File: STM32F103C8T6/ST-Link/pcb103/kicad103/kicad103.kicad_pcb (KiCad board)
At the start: 2 copper layers, 1 part, among them J1 0480372200

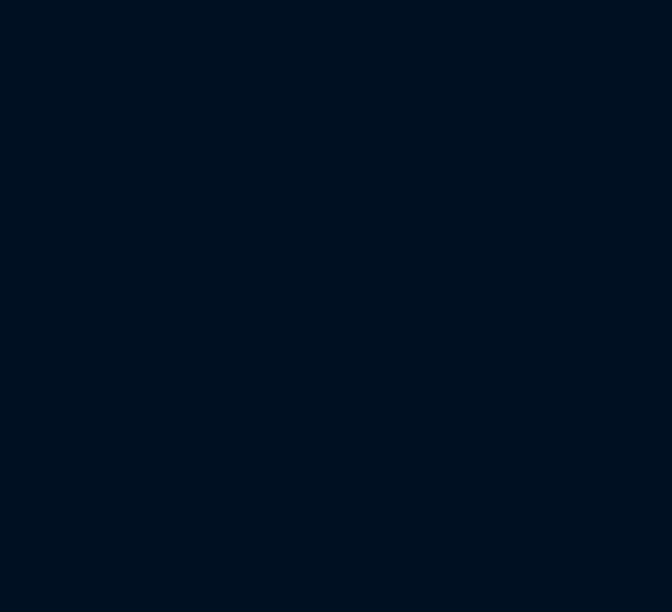
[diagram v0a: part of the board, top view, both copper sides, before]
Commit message: Add 3.3V LDO
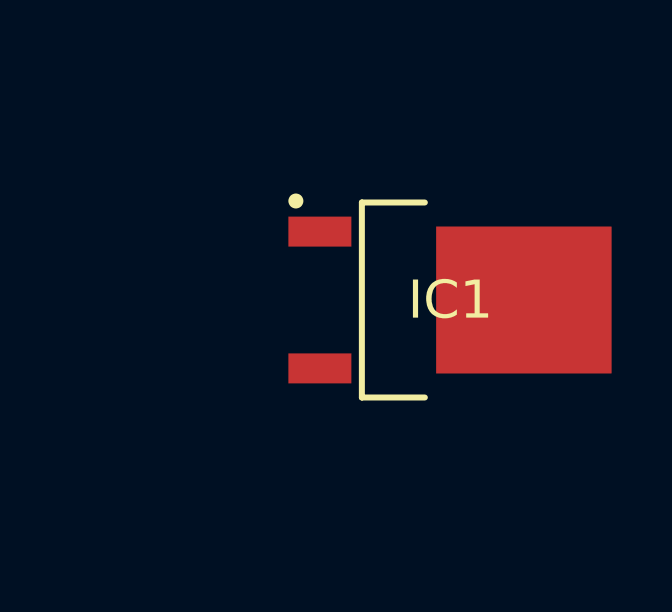
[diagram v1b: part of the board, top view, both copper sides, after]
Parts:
- added IC1: LD1117DT33TR, Library:TO228P972X240-3N, F.Cu at (236.3, 74.2)
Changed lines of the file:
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@@
   (net 7 "unconnected-(J1-Pad7)")
   (net 8 "unconnected-(J1-Pad8)")
+  (net 9 "unconnected-(IC1-GND-Pad1)")
+  (net 10 "unconnected-(IC1-VIN-Pad3)")
+  (net 11 "unconnected-(IC1-(THERMALPAD)-Pad4)")
+  (footprint "Library:TO228P972X240-3N" (layer "F.Cu")
+    (at 236.35 74.2)
+    (descr "DPAK (TO-252)")
+    (tags "Integrated Circuit")
+    (property "Arrow Part Number" "LD1117DT33TR")
+    (property "Arrow Price/Stock" "https://www.arrow.com/en/products/ld1117dt33tr/stmicroelectronics?region=nac")
+    (property "Height" "2.4")
+    (property "Manufacturer_Name" "STMicroelectronics")
+    (property "Manufacturer_Part_Number" "LD1117DT33TR")
+    (property "Mouser Part Number" "511-LD1117DT33-TR")
+    (property "Mouser Price/Stock" "https://www.mouser.co.uk/ProductDetail/STMicroelectronics/LD1117DT33TR?qs=4JhUBQGAOSd4P5jVYGxp2g%3D%3D")
+    (property "Sheetfile" "kicad103.kicad_sch")
+    (property "Sheetname" "")
+    (property "ki_description" "LDO Regulator 3.3V 1.3A DPAK STMicroelectronics LD1117DT33TR, LDO Voltage Regulator, 1.3A, 3.3 V +/-1%, 3-Pin DPAK")
+    (attr smd)
+    (fp_text reference "IC1" (at 0 0) (layer "F.SilkS")
+        (effects (font (size 1.27 1.27) (thickness 0.254)))
+    )
+    (fp_text value "LD1117DT33TR" (at 0 0) (layer "F.SilkS") hide
+        (effects (font (size 1.27 1.27) (thickness 0.254)))
+    )
+    (fp_text user "${REFERENCE}" (at 0 0) (layer "F.Fab")
+        (effects (font (size 1.27 1.27) (thickness 0.254)))
+    )
+    (fp_line (start -2.95 -3.25) (end -0.85 -3.25)
+      (stroke (width 0.2) (type solid)) (layer "F.SilkS"))
+    (fp_line (start -2.95 3.25) (end -2.95 -3.25)
+      (stroke (width 0.2) (type solid)) (layer "F.SilkS"))
+    (fp_line (start -0.85 3.25) (end -2.95 3.25)
+      (stroke (width 0.2) (type solid)) (layer "F.SilkS"))
+    (fp_circle (center -5.15 -3.3) (end -5.15 -3.175)
+      (stroke (width 0.25) (type solid)) (fill none) (layer "F.SilkS"))
+    (fp_line (start -5.65 -3.55) (end -5.65 3.55)
+      (stroke (width 0.05) (type solid)) (layer "F.CrtYd"))
+    (fp_line (start -5.65 3.55) (end 5.65 3.55)
+      (stroke (width 0.05) (type solid)) (layer "F.CrtYd"))
+    (fp_line (start -2.088 -3.3) (end -2.088 3.3)
+      (stroke (width 0.001) (type solid)) (layer "F.CrtYd"))
+    (fp_line (start -2.088 3.3) (end 4.112 3.3)
+      (stroke (width 0.001) (type solid)) (layer "F.CrtYd"))
+    (fp_line (start -0.5 0) (end 0.5 0)
+      (stroke (width 0.05) (type solid)) (layer "F.CrtYd"))
+    (fp_line (start 0 0.5) (end 0 -0.5)
+      (stroke (width 0.05) (type solid)) (layer "F.CrtYd"))
+    (fp_line (start 4.112 -3.3) (end -2.088 -3.3)
+      (stroke (width 0.001) (type solid)) (layer "F.CrtYd"))
+    (fp_line (start 4.112 3.3) (end 4.112 -3.3)
+      (stroke (width 0.001) (type solid)) (layer "F.CrtYd"))
+    (fp_line (start 5.65 -3.55) (end -5.65 -3.55)
+      (stroke (width 0.05) (type solid)) (layer "F.CrtYd"))
+    (fp_line (start 5.65 3.55) (end 5.65 -3.55)
+      (stroke (width 0.05) (type solid)) (layer "F.CrtYd"))
+    (fp_line (start -2.037 -3.25) (end -2.037 3.25)
+      (stroke (width 0.1) (type solid)) (layer "F.Fab"))
+    (fp_line (start -2.037 3.25) (end 4.062 3.25)
+      (stroke (width 0.1) (type solid)) (layer "F.Fab"))
+    (fp_line (start 4.062 -3.25) (end -2.037 -3.25)
+      (stroke (width 0.1) (type solid)) (layer "F.Fab"))
+    (fp_line (start 4.062 2.35) (end 4.326 2.35)
+      (stroke (width 0.1) (type solid)) (layer "F.Fab"))
+    (fp_line (start 4.062 3.25) (end 4.062 -3.25)
+      (stroke (width 0.1) (type solid)) (layer "F.Fab"))
+    (fp_line (start 4.326 2.35) (end 4.863 1.756)
+      (stroke (width 0.1) (type solid)) (layer "F.Fab"))
+    (fp_line (start 4.327 -2.35) (end 4.063 -2.35)
+      (stroke (width 0.1) (type solid)) (layer "F.Fab"))
+    (fp_line (start 4.863 -1.756) (end 4.327 -2.35)
+      (stroke (width 0.1) (type solid)) (layer "F.Fab"))
+    (fp_line (start 4.863 1.756) (end 4.863 -1.756)
+      (stroke (width 0.1) (type solid)) (layer "F.Fab"))
+    (pad "1" smd rect (at -4.35 -2.28 90) (size 1 2.1) (layers "F.Cu" "F.Paste" "F.Mask")
+      (net 9 "unconnected-(IC1-GND-Pad1)") (pinfunction "GND") (pintype "input"))
+    (pad "3" smd rect (at -4.35 2.28 90) (size 1 2.1) (layers "F.Cu" "F.Paste" "F.Mask")
+      (net 10 "unconnected-(IC1-VIN-Pad3)") (pinfunction "VIN") (pintype "output"))
+    (pad "4" smd rect (at 2.45 0 90) (size 4.9 5.85) (layers "F.Cu" "F.Paste" "F.Mask")
+      (net 11 "unconnected-(IC1-(THERMALPAD)-Pad4)") (pinfunction "(THERMALPAD)") (pintype "output"))
+    (model "/home/vovan/repos/bluepillfw/STM32F103C8T6/ST-Link/pcb103/mouser/lib/LD1117DT33TR.stp"
+      (offset (xyz 1.25 0 0))
+      (scale (xyz 1 1 1))
+      (rotate (xyz 0 0 90))
+    )
+  )
   (footprint "Library:0480372200" (layer "F.Cu")
     (at 211.95 77.375)

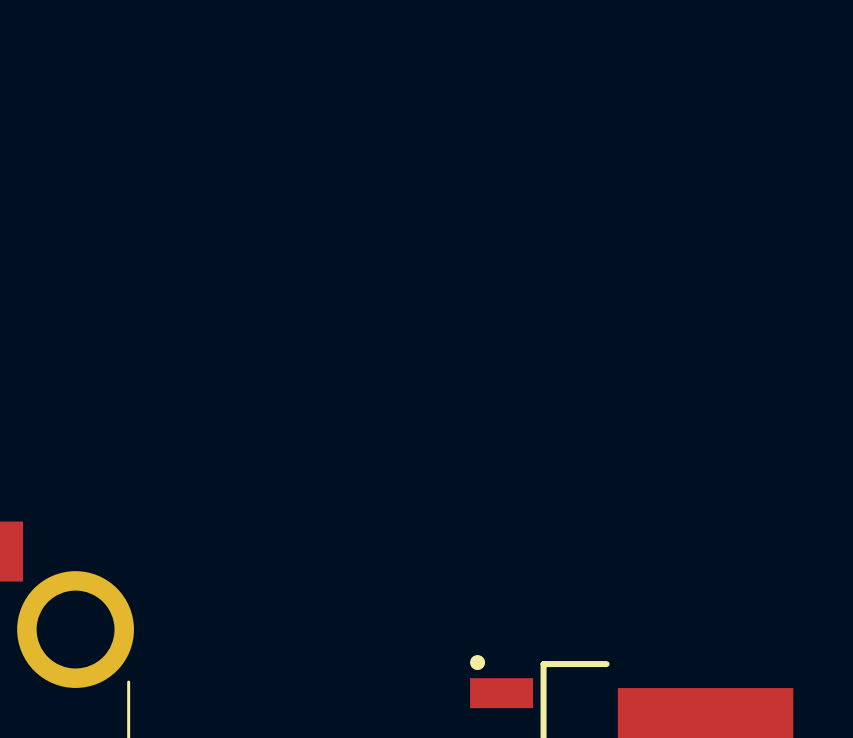
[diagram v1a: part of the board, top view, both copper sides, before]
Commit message: Add power LED
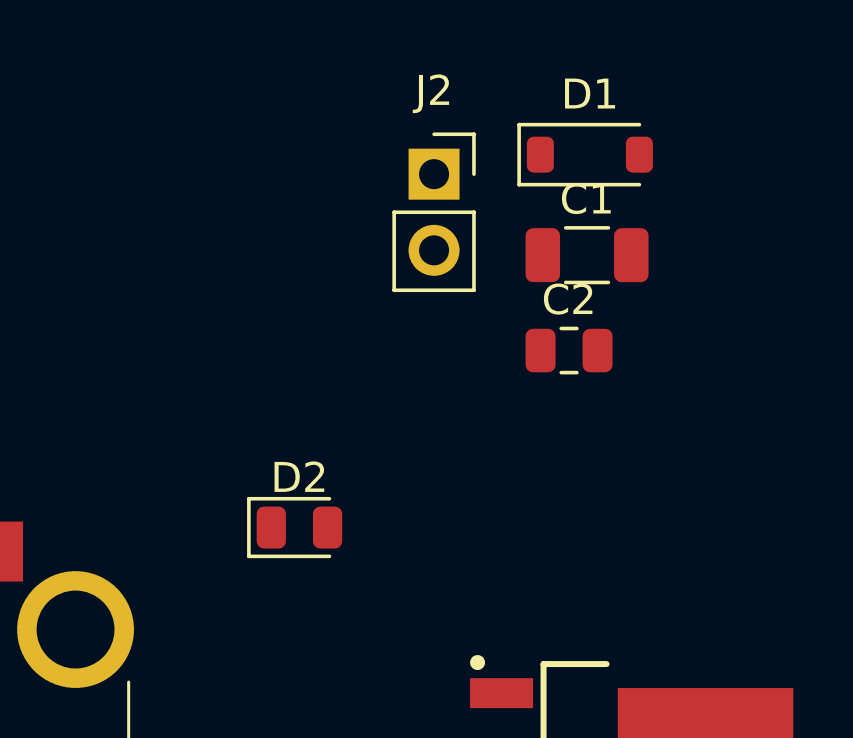
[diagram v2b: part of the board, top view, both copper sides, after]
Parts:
- added C1: 100n, Capacitor_SMD:C_1206_3216Metric, F.Cu at (234.8, 57.3)
- added C2: 10u, Capacitor_SMD:C_0805_2012Metric, F.Cu at (234.2, 60.5)
- added D1: D_Schottky, Diode_SMD:D_SOD-123, F.Cu at (234.9, 54.0)
- added D2: RED, LED_SMD:LED_0805_2012Metric, F.Cu at (225.3, 66.4)
- added J2: Conn_01x02_Socket, Connector_PinSocket_2.54mm:PinSocket_1x02_P2.54mm_Vertical, F.Cu at (229.8, 54.6)
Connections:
- IC1 pad 1: unconnected-(IC1-GND-Pad1) -> GND
- IC1 pad 3: unconnected-(IC1-VIN-Pad3) -> Net-(D1-K)
- IC1 pad 4: unconnected-(IC1-(THERMALPAD)-Pad4) -> /3.3V
- J1 pad 1: unconnected-(J1-Pad1) -> +5V
- J1 pad 4: unconnected-(J1-Pad4) -> GND

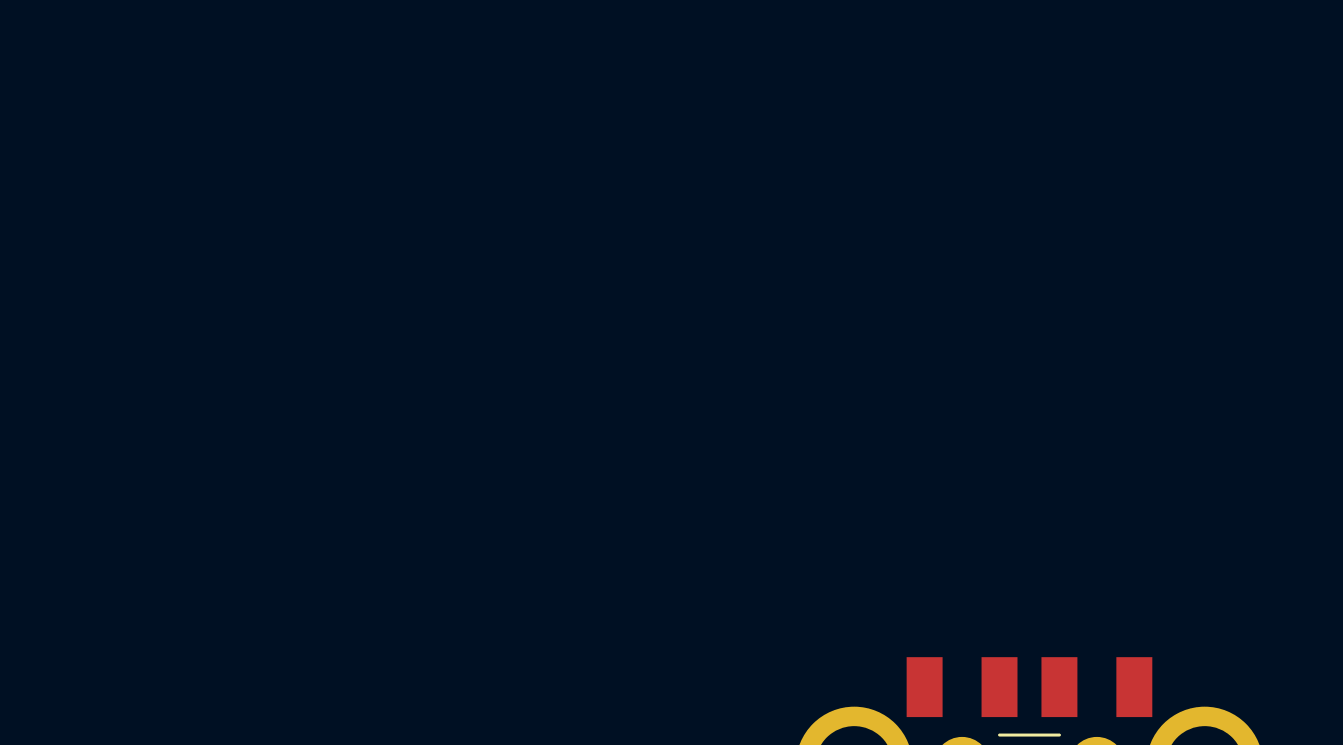
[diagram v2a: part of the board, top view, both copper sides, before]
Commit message: Add status LED
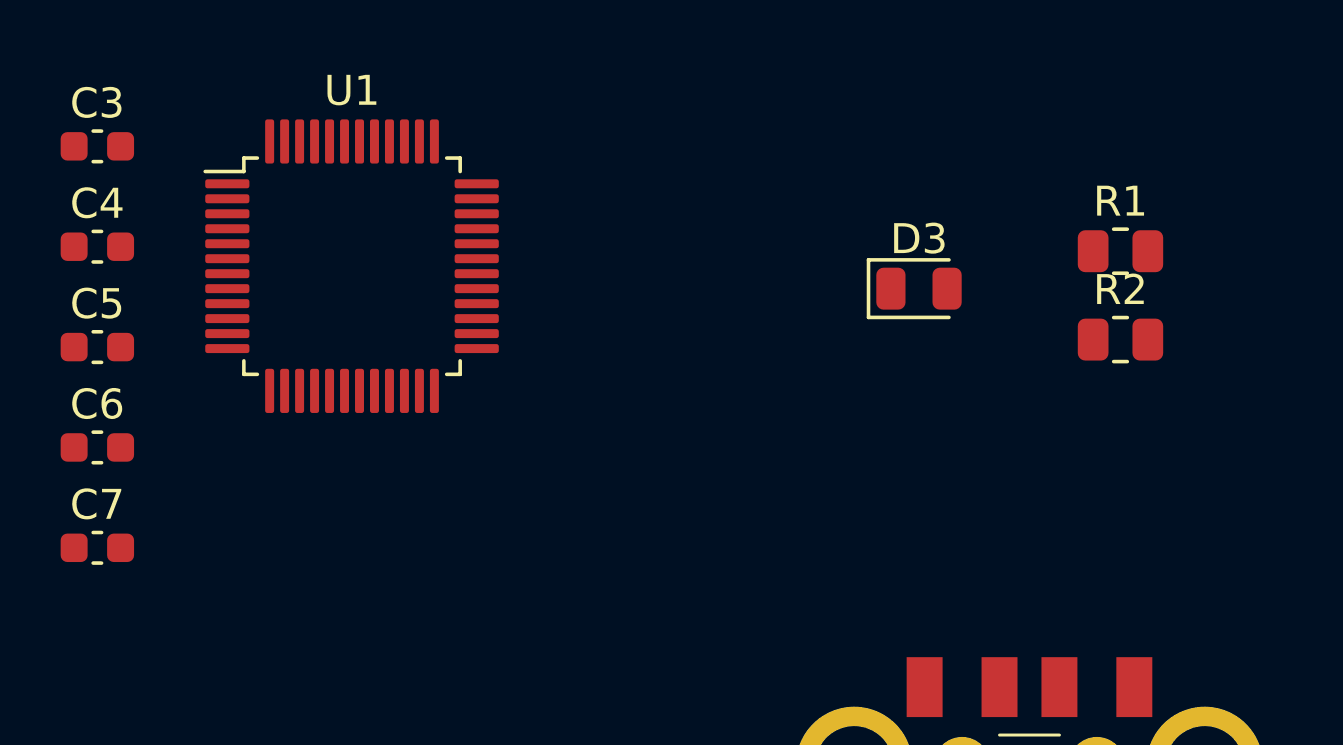
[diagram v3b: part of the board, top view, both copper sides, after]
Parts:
- added C3: 100n, Capacitor_SMD:C_0603_1608Metric, F.Cu at (180.8, 49.1)
- added C4: 100n, Capacitor_SMD:C_0603_1608Metric, F.Cu at (180.8, 52.5)
- added C5: 100n, Capacitor_SMD:C_0603_1608Metric, F.Cu at (180.8, 55.9)
- added C6: 100n, Capacitor_SMD:C_0603_1608Metric, F.Cu at (180.8, 59.2)
- added C7: 100n, Capacitor_SMD:C_0603_1608Metric, F.Cu at (180.8, 62.5)
- added D3: YELLOW, LED_SMD:LED_0805_2012Metric, F.Cu at (208.3, 53.9)
- added R1: 1k5, Resistor_SMD:R_0805_2012Metric, F.Cu at (215.0, 52.6)
- added R2: 1k5, Resistor_SMD:R_0805_2012Metric, F.Cu at (215.0, 55.6)
- added U1: STM32F103C8T6, Package_QFP:LQFP-48_7x7mm_P0.5mm, F.Cu at (189.3, 53.1)
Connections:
- D2 pad 1: GND -> Net-(D2-K)
- J1 pad 2: unconnected-(J1-Pad2) -> /USB_D-
- J1 pad 3: unconnected-(J1-Pad3) -> /USB_D+
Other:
- copper layers 2 -> 4

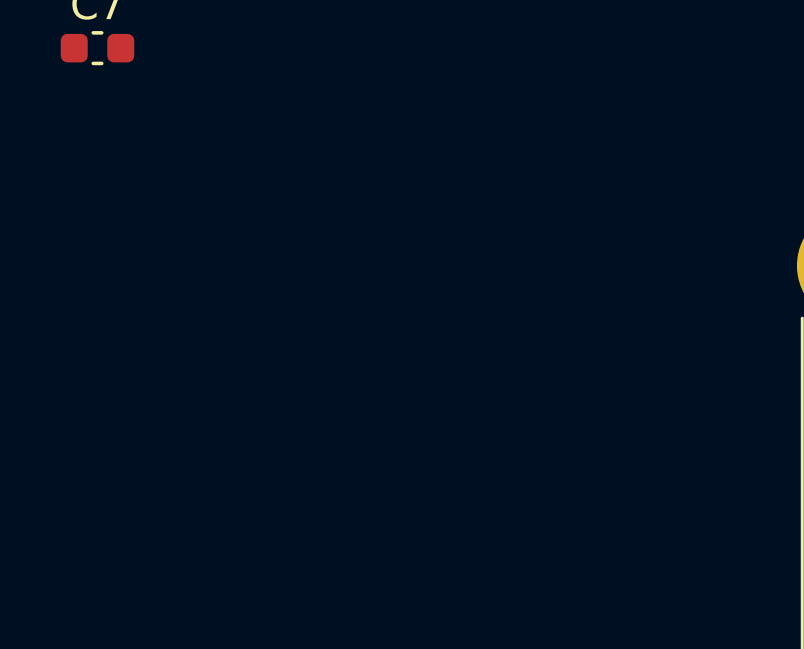
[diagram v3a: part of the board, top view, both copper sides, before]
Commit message: Add 8MHz crystal
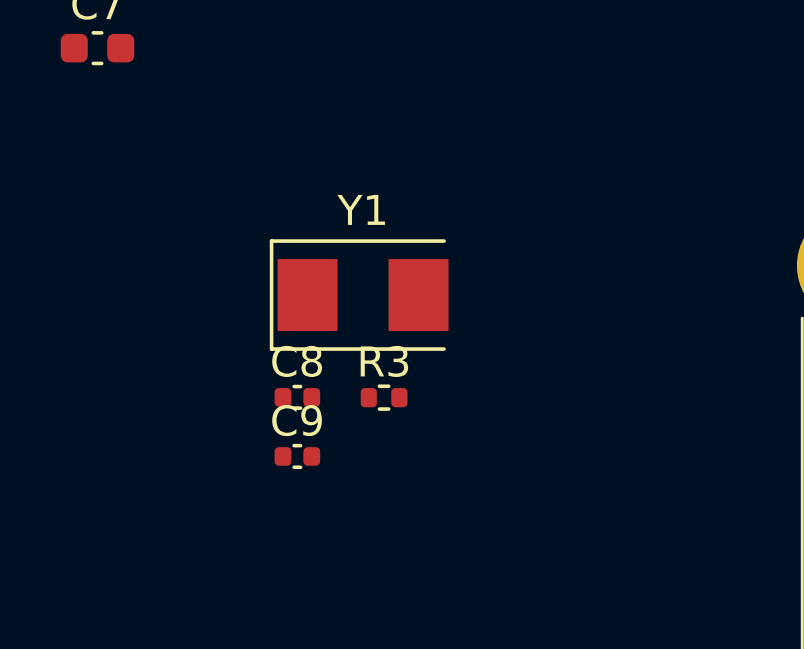
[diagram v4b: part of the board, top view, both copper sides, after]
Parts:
- added C8: 27p, Capacitor_SMD:C_0402_1005Metric, F.Cu at (187.5, 74.2)
- added C9: 27p, Capacitor_SMD:C_0402_1005Metric, F.Cu at (187.5, 76.2)
- added R3: 47, Resistor_SMD:R_0402_1005Metric, F.Cu at (190.4, 74.2)
- added Y1: 8MHz 20pF, Crystal:Crystal_SMD_5032-2Pin_5.0x3.2mm, F.Cu at (189.7, 70.8)
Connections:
- U1 pad 5: unconnected-(U1-PD0-Pad5) -> Net-(U1-PD0)
- U1 pad 6: unconnected-(U1-PD1-Pad6) -> Net-(U1-PD1)
